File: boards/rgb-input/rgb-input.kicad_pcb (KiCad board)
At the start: 2 copper layers, 184.5 x 137 mm, 80 parts, among them J1 Conn_01x03, J10 Conn_01x03, J11 Conn_01x03, J12 Conn_01x03, J13 I2C, J14 N2K, J15 Conn_01x03, J16 Conn_01x03, J17 Conn_01x03, J18 Conn_01x03, J2 Conn_01x03, J3 Conn_01x03, J5 Conn_01x03, J6 Conn_01x03, J7 Conn_01x03, J8 Conn_01x03, J9 Conn_01x03, U1 ESP32-DEVKITC, U13 MCP1502, U2 MCP3208, U3 R-78K5.0-1.0, U4 MCP3221A0T

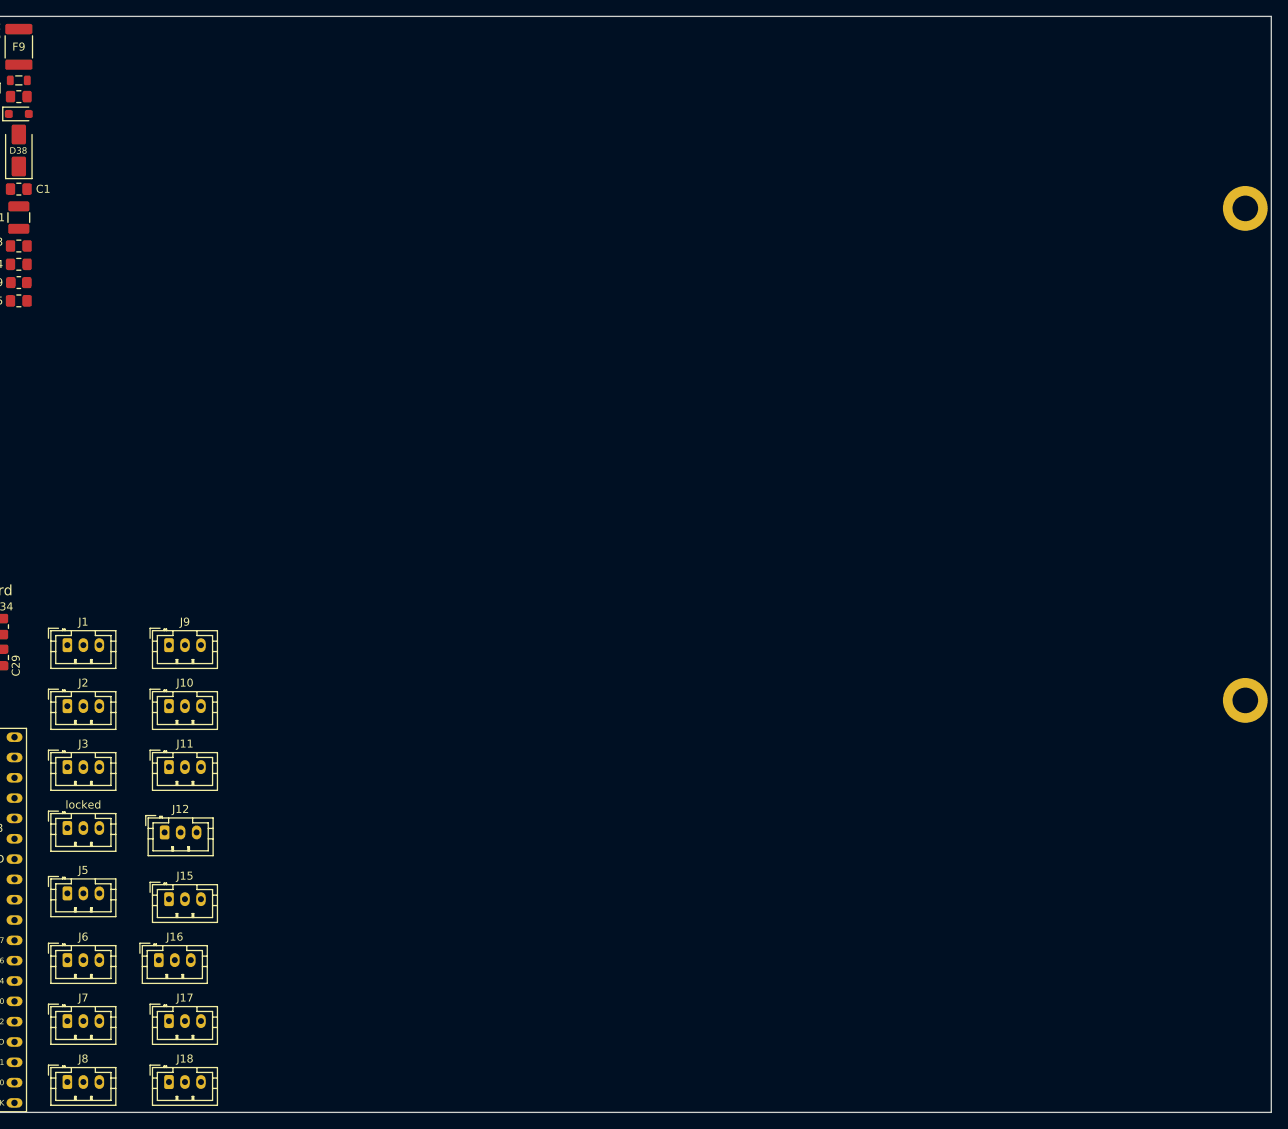
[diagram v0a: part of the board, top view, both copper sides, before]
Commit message: input board shaping up to be lit.
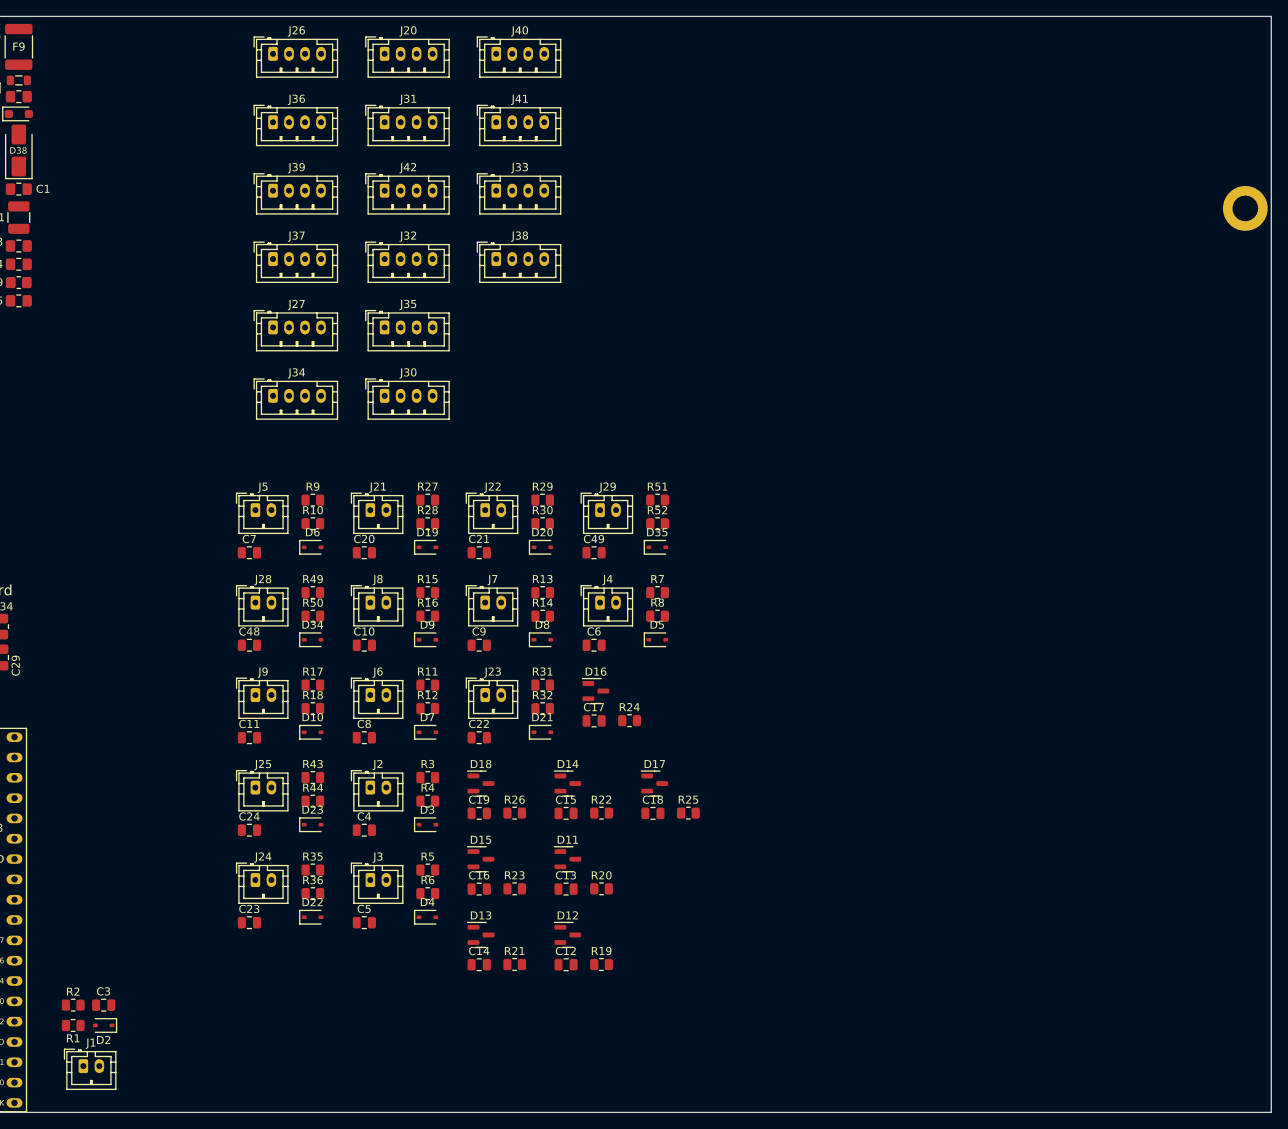
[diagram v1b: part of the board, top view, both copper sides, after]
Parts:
- removed H5: MountingHole, MountingHole:MountingHole_3.2mm_M3_DIN965_Pad
- removed J10, J11, J12, J15, J16, J17, J18, locked: Conn_01x03, Connector_JST:JST_PH_B3B-PH-K_1x03_P2.00mm_Vertical
- added C10: 0.01uf, Capacitor_SMD:C_0805_2012Metric, F.Cu at (71.1, 78.6)
- added C11: 0.01uf, Capacitor_SMD:C_0805_2012Metric, F.Cu at (56.8, 90.2)
- added C12: 0.01uf, Capacitor_SMD:C_0805_2012Metric, F.Cu at (96.3, 118.5)
- added C13: 0.01uf, Capacitor_SMD:C_0805_2012Metric, F.Cu at (96.3, 109.1)
- added C14: 0.01uf, Capacitor_SMD:C_0805_2012Metric, F.Cu at (85.5, 118.5)
- added C15: 0.01uf, Capacitor_SMD:C_0805_2012Metric, F.Cu at (96.3, 99.6)
- added C16: 0.01uf, Capacitor_SMD:C_0805_2012Metric, F.Cu at (85.5, 109.1)
- added C17: 0.01uf, Capacitor_SMD:C_0805_2012Metric, F.Cu at (99.8, 88.1)
- added C18: 0.01uf, Capacitor_SMD:C_0805_2012Metric, F.Cu at (107.2, 99.6)
- added C19: 0.01uf, Capacitor_SMD:C_0805_2012Metric, F.Cu at (85.5, 99.6)
- added C20: 0.01uf, Capacitor_SMD:C_0805_2012Metric, F.Cu at (71.1, 67.0)
- added C21: 0.01uf, Capacitor_SMD:C_0805_2012Metric, F.Cu at (85.5, 67.0)
- added C22: 0.01uf, Capacitor_SMD:C_0805_2012Metric, F.Cu at (85.5, 90.2)
- added C23: 0.01uf, Capacitor_SMD:C_0805_2012Metric, F.Cu at (56.8, 113.3)
- added C24: 0.01uf, Capacitor_SMD:C_0805_2012Metric, F.Cu at (56.8, 101.7)
- added C3: 0.01uf, Capacitor_SMD:C_0805_2012Metric, F.Cu at (38.5, 123.6)
- added C4: 0.01uf, Capacitor_SMD:C_0805_2012Metric, F.Cu at (71.1, 101.7)
- added C48: 0.01uf, Capacitor_SMD:C_0805_2012Metric, F.Cu at (56.8, 78.6)
- added C49: 0.01uf, Capacitor_SMD:C_0805_2012Metric, F.Cu at (99.8, 67.0)
- added C5: 0.01uf, Capacitor_SMD:C_0805_2012Metric, F.Cu at (71.1, 113.3)
- added C6: 0.01uf, Capacitor_SMD:C_0805_2012Metric, F.Cu at (99.8, 78.6)
- added C7: 0.01uf, Capacitor_SMD:C_0805_2012Metric, F.Cu at (56.8, 67.0)
- added C8: 0.01uf, Capacitor_SMD:C_0805_2012Metric, F.Cu at (71.1, 90.2)
- added C9: 0.01uf, Capacitor_SMD:C_0805_2012Metric, F.Cu at (85.5, 78.6)
- added D10: PESD3V3L1BA, Diode_SMD:D_SOD-323, F.Cu at (64.7, 89.5)
- added D11: BAT54S, Package_TO_SOT_SMD:SOT-23, F.Cu at (96.6, 105.4)
- added D12: BAT54S, Package_TO_SOT_SMD:SOT-23, F.Cu at (96.6, 114.8)
- added D13: BAT54S, Package_TO_SOT_SMD:SOT-23, F.Cu at (85.7, 114.8)
- added D14: BAT54S, Package_TO_SOT_SMD:SOT-23, F.Cu at (96.6, 95.9)
- added D15: BAT54S, Package_TO_SOT_SMD:SOT-23, F.Cu at (85.7, 105.4)
- added D16: BAT54S, Package_TO_SOT_SMD:SOT-23, F.Cu at (100.1, 84.3)
- added D17: BAT54S, Package_TO_SOT_SMD:SOT-23, F.Cu at (107.4, 95.9)
- added D18: BAT54S, Package_TO_SOT_SMD:SOT-23, F.Cu at (85.7, 95.9)
- added D19: PESD3V3L1BA, Diode_SMD:D_SOD-323, F.Cu at (79.0, 66.4)
- added D2: PESD3V3L1BA, Diode_SMD:D_SOD-323, F.Cu at (38.5, 126.1)
- added D20: PESD3V3L1BA, Diode_SMD:D_SOD-323, F.Cu at (93.4, 66.4)
- added D21: PESD3V3L1BA, Diode_SMD:D_SOD-323, F.Cu at (93.4, 89.5)
- added D22: PESD3V3L1BA, Diode_SMD:D_SOD-323, F.Cu at (64.7, 112.6)
- added D23: PESD3V3L1BA, Diode_SMD:D_SOD-323, F.Cu at (64.7, 101.0)
- added D3: PESD3V3L1BA, Diode_SMD:D_SOD-323, F.Cu at (79.0, 101.0)
- added D34: PESD3V3L1BA, Diode_SMD:D_SOD-323, F.Cu at (64.7, 77.9)
- added D35: PESD3V3L1BA, Diode_SMD:D_SOD-323, F.Cu at (107.7, 66.4)
- added D4: PESD3V3L1BA, Diode_SMD:D_SOD-323, F.Cu at (79.0, 112.6)
- added D5: PESD3V3L1BA, Diode_SMD:D_SOD-323, F.Cu at (107.7, 77.9)
- added D6: PESD3V3L1BA, Diode_SMD:D_SOD-323, F.Cu at (64.7, 66.4)
- added D7: PESD3V3L1BA, Diode_SMD:D_SOD-323, F.Cu at (79.0, 89.5)
- added D8: PESD3V3L1BA, Diode_SMD:D_SOD-323, F.Cu at (93.4, 77.9)
- added D9: PESD3V3L1BA, Diode_SMD:D_SOD-323, F.Cu at (79.0, 77.9)
- added J20: Conn_01x04, Connector_JST:JST_PH_B4B-PH-K_1x04_P2.00mm_Vertical, F.Cu at (73.7, 4.68)
- added J21: Conn_01x02, Connector_JST:JST_PH_B2B-PH-K_1x02_P2.00mm_Vertical, F.Cu at (71.9, 61.7)
- added J22: Conn_01x02, Connector_JST:JST_PH_B2B-PH-K_1x02_P2.00mm_Vertical, F.Cu at (86.2, 61.7)
- added J23: Conn_01x02, Connector_JST:JST_PH_B2B-PH-K_1x02_P2.00mm_Vertical, F.Cu at (86.2, 84.8)
- added J24: Conn_01x02, Connector_JST:JST_PH_B2B-PH-K_1x02_P2.00mm_Vertical, F.Cu at (57.5, 108.0)
- added J25: Conn_01x02, Connector_JST:JST_PH_B2B-PH-K_1x02_P2.00mm_Vertical, F.Cu at (57.5, 96.4)
- added J26: Conn_01x04, Connector_JST:JST_PH_B4B-PH-K_1x04_P2.00mm_Vertical, F.Cu at (59.7, 4.68)
- added J27: Conn_01x04, Connector_JST:JST_PH_B4B-PH-K_1x04_P2.00mm_Vertical, F.Cu at (59.7, 38.9)
- added J28: Conn_01x02, Connector_JST:JST_PH_B2B-PH-K_1x02_P2.00mm_Vertical, F.Cu at (57.5, 73.3)
- added J29: Conn_01x02, Connector_JST:JST_PH_B2B-PH-K_1x02_P2.00mm_Vertical, F.Cu at (100.6, 61.7)
- added J30: Conn_01x04, Connector_JST:JST_PH_B4B-PH-K_1x04_P2.00mm_Vertical, F.Cu at (73.7, 47.4)
- added J31: Conn_01x04, Connector_JST:JST_PH_B4B-PH-K_1x04_P2.00mm_Vertical, F.Cu at (73.7, 13.2)
- added J32: Conn_01x04, Connector_JST:JST_PH_B4B-PH-K_1x04_P2.00mm_Vertical, F.Cu at (73.7, 30.3)
- added J33: Conn_01x04, Connector_JST:JST_PH_B4B-PH-K_1x04_P2.00mm_Vertical, F.Cu at (87.6, 21.8)
- added J34: Conn_01x04, Connector_JST:JST_PH_B4B-PH-K_1x04_P2.00mm_Vertical, F.Cu at (59.7, 47.4)
- added J35: Conn_01x04, Connector_JST:JST_PH_B4B-PH-K_1x04_P2.00mm_Vertical, F.Cu at (73.7, 38.9)
- added J36: Conn_01x04, Connector_JST:JST_PH_B4B-PH-K_1x04_P2.00mm_Vertical, F.Cu at (59.7, 13.2)
- added J37: Conn_01x04, Connector_JST:JST_PH_B4B-PH-K_1x04_P2.00mm_Vertical, F.Cu at (59.7, 30.3)
- added J38: Conn_01x04, Connector_JST:JST_PH_B4B-PH-K_1x04_P2.00mm_Vertical, F.Cu at (87.6, 30.3)
- added J39: Conn_01x04, Connector_JST:JST_PH_B4B-PH-K_1x04_P2.00mm_Vertical, F.Cu at (59.7, 21.8)
- added J4: Conn_01x02, Connector_JST:JST_PH_B2B-PH-K_1x02_P2.00mm_Vertical, F.Cu at (100.6, 73.3)
- added J40: Conn_01x04, Connector_JST:JST_PH_B4B-PH-K_1x04_P2.00mm_Vertical, F.Cu at (87.6, 4.68)
- added J41: Conn_01x04, Connector_JST:JST_PH_B4B-PH-K_1x04_P2.00mm_Vertical, F.Cu at (87.6, 13.2)
- added J42: Conn_01x04, Connector_JST:JST_PH_B4B-PH-K_1x04_P2.00mm_Vertical, F.Cu at (73.7, 21.8)
- added R1: 1k, Resistor_SMD:R_0805_2012Metric, F.Cu at (34.7, 126.1)
- added R10: 100k, Resistor_SMD:R_0805_2012Metric, F.Cu at (64.7, 63.4)
- added R11: 1k, Resistor_SMD:R_0805_2012Metric, F.Cu at (79.1, 83.6)
- added R12: 100k, Resistor_SMD:R_0805_2012Metric, F.Cu at (79.1, 86.5)
- added R13: 1k, Resistor_SMD:R_0805_2012Metric, F.Cu at (93.4, 72.0)
- added R14: 100k, Resistor_SMD:R_0805_2012Metric, F.Cu at (93.4, 75.0)
- added R15: 1k, Resistor_SMD:R_0805_2012Metric, F.Cu at (79.1, 72.0)
- added R16: 100k, Resistor_SMD:R_0805_2012Metric, F.Cu at (79.1, 75.0)
- added R17: 1k, Resistor_SMD:R_0805_2012Metric, F.Cu at (64.7, 83.6)
- added R18: 100k, Resistor_SMD:R_0805_2012Metric, F.Cu at (64.7, 86.5)
- added R19: 1k, Resistor_SMD:R_0805_2012Metric, F.Cu at (100.8, 118.5)
- added R2: 100k, Resistor_SMD:R_0805_2012Metric, F.Cu at (34.7, 123.6)
- added R20: 1k, Resistor_SMD:R_0805_2012Metric, F.Cu at (100.8, 109.1)
- added R21: 1k, Resistor_SMD:R_0805_2012Metric, F.Cu at (89.9, 118.5)
- added R22: 1k, Resistor_SMD:R_0805_2012Metric, F.Cu at (100.8, 99.6)
- added R23: 1k, Resistor_SMD:R_0805_2012Metric, F.Cu at (89.9, 109.1)
- added R24: 1k, Resistor_SMD:R_0805_2012Metric, F.Cu at (104.3, 88.0)
- added R25: 1k, Resistor_SMD:R_0805_2012Metric, F.Cu at (111.6, 99.6)
- added R26: 1k, Resistor_SMD:R_0805_2012Metric, F.Cu at (89.9, 99.6)
- added R27: 1k, Resistor_SMD:R_0805_2012Metric, F.Cu at (79.1, 60.5)
- added R28: 100k, Resistor_SMD:R_0805_2012Metric, F.Cu at (79.1, 63.4)
- added R29: 1k, Resistor_SMD:R_0805_2012Metric, F.Cu at (93.4, 60.5)
- added R3: 1k, Resistor_SMD:R_0805_2012Metric, F.Cu at (79.1, 95.1)
- added R30: 100k, Resistor_SMD:R_0805_2012Metric, F.Cu at (93.4, 63.4)
- added R31: 1k, Resistor_SMD:R_0805_2012Metric, F.Cu at (93.4, 83.6)
- added R32: 100k, Resistor_SMD:R_0805_2012Metric, F.Cu at (93.4, 86.5)
- added R35: 1k, Resistor_SMD:R_0805_2012Metric, F.Cu at (64.7, 106.7)
- added R36: 100k, Resistor_SMD:R_0805_2012Metric, F.Cu at (64.7, 109.7)
- added R4: 100k, Resistor_SMD:R_0805_2012Metric, F.Cu at (79.1, 98.1)
- added R43: 1k, Resistor_SMD:R_0805_2012Metric, F.Cu at (64.7, 95.1)
- added R44: 100k, Resistor_SMD:R_0805_2012Metric, F.Cu at (64.7, 98.1)
- added R49: 1k, Resistor_SMD:R_0805_2012Metric, F.Cu at (64.7, 72.0)
- added R5: 1k, Resistor_SMD:R_0805_2012Metric, F.Cu at (79.1, 106.7)
- added R50: 100k, Resistor_SMD:R_0805_2012Metric, F.Cu at (64.7, 75.0)
- added R51: 1k, Resistor_SMD:R_0805_2012Metric, F.Cu at (107.8, 60.5)
- added R52: 100k, Resistor_SMD:R_0805_2012Metric, F.Cu at (107.8, 63.4)
- added R6: 100k, Resistor_SMD:R_0805_2012Metric, F.Cu at (79.1, 109.7)
- added R7: 1k, Resistor_SMD:R_0805_2012Metric, F.Cu at (107.8, 72.0)
- added R8: 100k, Resistor_SMD:R_0805_2012Metric, F.Cu at (107.8, 75.0)
- added R9: 1k, Resistor_SMD:R_0805_2012Metric, F.Cu at (64.7, 60.5)
- J1, J2, J3, J5, J6, J7, J8, J9: value Conn_01x03 -> Conn_01x02; footprint Connector_JST:JST_PH_B3B-PH-K_1x03_P2.00mm_Vertical -> Connector_JST:JST_PH_B2B-PH-K_1x02_P2.00mm_Vertical
- moved J7 73.9 mm to (86.2, 73.3)
- moved J8 70.9 mm to (71.9, 73.3)
- moved J5 53.4 mm to (57.5, 61.7)
- moved J1 52.7 mm to (36.0, 131.2)
- moved J6 50.3 mm to (71.9, 84.8)
- moved J3 40.4 mm to (71.9, 108.0)
- moved J2 39.2 mm to (71.9, 96.4)
- moved J9 12.5 mm to (57.5, 84.8)
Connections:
- J1 pad 1: unconnected-(J1-Pin_1-Pad1) -> Net-(D2-A2)
- J1 pad 2: unconnected-(J1-Pin_2-Pad2) -> GNDD
- J2 pad 1: unconnected-(J2-Pin_1-Pad1) -> Net-(D3-A2)
- J2 pad 2: unconnected-(J2-Pin_2-Pad2) -> GNDD
- J3 pad 1: unconnected-(J3-Pin_1-Pad1) -> Net-(D4-A2)
- J3 pad 2: unconnected-(J3-Pin_2-Pad2) -> GNDD
- J5 pad 1: unconnected-(J5-Pin_1-Pad1) -> Net-(D6-A2)
- J5 pad 2: unconnected-(J5-Pin_2-Pad2) -> GNDD
- J6 pad 1: unconnected-(J6-Pin_1-Pad1) -> Net-(D7-A2)
- J6 pad 2: unconnected-(J6-Pin_2-Pad2) -> GNDD
- J7 pad 1: unconnected-(J7-Pin_1-Pad1) -> Net-(D8-A2)
- J7 pad 2: unconnected-(J7-Pin_2-Pad2) -> GNDD
- J8 pad 1: unconnected-(J8-Pin_1-Pad1) -> Net-(D9-A2)
- J8 pad 2: unconnected-(J8-Pin_2-Pad2) -> GNDD
- J9 pad 1: unconnected-(J9-Pin_1-Pad1) -> Net-(D10-A2)
- J9 pad 2: unconnected-(J9-Pin_2-Pad2) -> GNDD
- U1 pad 10: unconnected-(U1-GPIO26-Pad10) -> /Input Switch7/INPUT
- U1 pad 11: unconnected-(U1-GPIO27-Pad11) -> /Input Switch8/INPUT
- U1 pad 12: unconnected-(U1-GPIO14-Pad12) -> /Input Switch9/INPUT
- U1 pad 13: unconnected-(U1-GPIO12-Pad13) -> /Input Switch10/INPUT
- U1 pad 15: unconnected-(U1-GPIO13-Pad15) -> /Input Switch11/INPUT
- U1 pad 24: unconnected-(U1-GPIO2-Pad24) -> /Input Switch12/INPUT
- U1 pad 26: CAN_RX -> /Input Switch13/INPUT
- U1 pad 27: unconnected-(U1-GPIO16-Pad27) -> /Input Switch14/INPUT
- U1 pad 29: CAN_TX -> /Input Switch15/INPUT
- U1 pad 3: unconnected-(U1-GPIO36-Pad3) -> /Input Switch0/INPUT
- U1 pad 4: unconnected-(U1-GPIO39-Pad4) -> /Input Switch1/INPUT
- U1 pad 5: unconnected-(U1-GPIO34-Pad5) -> /Input Switch2/INPUT
- U1 pad 6: unconnected-(U1-GPIO35-Pad6) -> /Input Switch3/INPUT
- U1 pad 7: unconnected-(U1-GPIO32-Pad7) -> /Input Switch4/INPUT
- U1 pad 8: unconnected-(U1-GPIO33-Pad8) -> /Input Switch5/INPUT
- U1 pad 9: unconnected-(U1-GPIO25-Pad9) -> /Input Switch6/INPUT
- U2 pad 1: /ADC/A0 -> /ADC Input/INPUT
- U2 pad 2: /ADC/A1 -> /ADC Input1/INPUT
- U2 pad 3: /ADC/A2 -> /ADC Input2/INPUT
- U2 pad 4: /ADC/A3 -> /ADC Input3/INPUT
- U2 pad 5: /ADC/A4 -> /ADC Input4/INPUT
- U2 pad 6: /ADC/A5 -> /ADC Input5/INPUT
- U2 pad 7: /ADC/A6 -> /ADC Input6/INPUT
- U2 pad 8: /ADC/A7 -> /ADC Input7/INPUT

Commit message: some adc changes and then rerouting
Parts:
- removed C38, C40, C41: 33pF, Capacitor_SMD:C_0805_2012Metric_Pad1.18x1.45mm_HandSolder
- removed C39, C42: 10uF, Capacitor_SMD:C_0805_2012Metric_Pad1.18x1.45mm_HandSolder
- removed D29, D30, D31: PESD5V0L1BA, Diode_SMD:D_SOD-323_HandSoldering
- removed FB4, FB5, FB6: GZ2012D601TF, Inductor_SMD:L_0805_2012Metric
- removed J42: Conn_01x04, Connector_JST:JST_PH_B4B-PH-K_1x04_P2.00mm_Vertical
- removed U4: MCP3221A0T, Package_TO_SOT_SMD:SOT-23-5
- added C25: 10uF, Capacitor_SMD:C_0805_2012Metric, F.Cu at (-22.4, 36.6)
- added C26: 10uF, Capacitor_SMD:C_0805_2012Metric, F.Cu at (-22.4, 51.2)
- added D39: BAT54S, Package_TO_SOT_SMD:SOT-23, F.Cu at (-15.7, 50.5)
- added JP1: SolderJumper_2_Open, Jumper:SolderJumper-2_P1.3mm_Open_RoundedPad1.0x1.5mm, F.Cu at (-11.1, 50.0)
- added R45: 10k, Resistor_SMD:R_0805_2012Metric, F.Cu at (-22.4, 30.6)
- added R46: 3.3k, Resistor_SMD:R_0805_2012Metric, F.Cu at (-22.4, 33.6)
- added R47: 10k, Resistor_SMD:R_0805_2012Metric, F.Cu at (-22.4, 45.3)
- added R48: 3.3k, Resistor_SMD:R_0805_2012Metric, F.Cu at (-22.4, 48.2)
- added U15: MCP3425A0T-ECH, Package_TO_SOT_SMD:SOT-23-6, F.Cu at (-15.6, 46.0)
- added U5: TLC5947DAP, Package_SO:HTSSOP-32-1EP_6.1x11mm_P0.65mm_EP5.2x11mm_Mask4.11x4.36mm_ThermalVias, F.Cu at (-29.7, 35.5)
- added U6: TLC5947DAP, Package_SO:HTSSOP-32-1EP_6.1x11mm_P0.65mm_EP5.2x11mm_Mask4.11x4.36mm_ThermalVias, F.Cu at (-29.7, 50.1)
- C37: value 33pF -> 10uF
- D1, D27, D28: value PESD5V0L1BA -> PESD3V3L1BA
- J14: value N2K -> Conn_01x04; footprint Connector_PinHeader_2.54mm:PinHeader_1x04_P2.54mm_Vertical -> Connector_JST:JST_PH_B4B-PH-K_1x04_P2.00mm_Vertical
- R33: value 130K 0.1% -> 300K 0.1%
- R34: value 15K 0.1% -> 22K 0.1%
- moved J14 71.7 mm to (73.6, 21.4), turned to 0 degrees
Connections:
- C29 pad 1: +3.3V -> ESP32_5V
- C37 pad 1: Net-(D29-A2) -> REF_3V3
- C37 pad 2: GNDD -> GNDA
- J14 pad 1: Net-(D29-A2) -> +5V
- J14 pad 2: Net-(D30-A2) -> /LEDS/LED Driver1/OUT6
- J14 pad 3: GNDD -> /LEDS/LED Driver1/OUT7
- J14 pad 4: Net-(D31-A2) -> /LEDS/LED Driver1/OUT8
- J20 pad 2: /RGB Output0/RED -> /LEDS/LED Driver1/OUT15
- J20 pad 3: /RGB Output0/GREEN -> /LEDS/LED Driver1/OUT16
- J20 pad 4: /RGB Output0/BLUE -> /LEDS/LED Driver1/OUT17
- J26 pad 2: /RGB Output1/RED -> /LEDS/LED Driver1/OUT3
- J26 pad 3: /RGB Output1/GREEN -> /LEDS/LED Driver1/OUT4
- J26 pad 4: /RGB Output1/BLUE -> /LEDS/LED Driver1/OUT5
- J27 pad 2: /RGB Output2/RED -> /LEDS/LED Driver/OUT6
- J27 pad 3: /RGB Output2/GREEN -> /LEDS/LED Driver/OUT7
- J27 pad 4: /RGB Output2/BLUE -> /LEDS/LED Driver/OUT8
- J30 pad 2: /RGB Output3/RED -> /LEDS/LED Driver1/OUT18
- J30 pad 3: /RGB Output3/GREEN -> /LEDS/LED Driver1/OUT19
- J30 pad 4: /RGB Output3/BLUE -> /LEDS/LED Driver1/OUT20
- J31 pad 2: /RGB Output5/RED -> /LEDS/LED Driver/OUT15
- J31 pad 3: /RGB Output5/GREEN -> /LEDS/LED Driver/OUT16
- J31 pad 4: /RGB Output5/BLUE -> /LEDS/LED Driver/OUT17
- J32 pad 2: /RGB Output4/RED -> /LEDS/LED Driver1/OUT12
- J32 pad 3: /RGB Output4/GREEN -> /LEDS/LED Driver1/OUT13
- J32 pad 4: /RGB Output4/BLUE -> /LEDS/LED Driver1/OUT14
- J33 pad 2: /RGB Output7/RED -> /LEDS/LED Driver/OUT3
- J33 pad 3: /RGB Output7/GREEN -> /LEDS/LED Driver/OUT4
- J33 pad 4: /RGB Output7/BLUE -> /LEDS/LED Driver/OUT5
- J34 pad 2: /RGB Output6/RED -> /LEDS/LED Driver/OUT18
- J34 pad 3: /RGB Output6/GREEN -> /LEDS/LED Driver/OUT19
- J34 pad 4: /RGB Output6/BLUE -> /LEDS/LED Driver/OUT20
- J35 pad 2: /RGB Output9/RED -> /LEDS/LED Driver/OUT12
- J35 pad 3: /RGB Output9/GREEN -> /LEDS/LED Driver/OUT13
- J35 pad 4: /RGB Output9/BLUE -> /LEDS/LED Driver/OUT14
- J36 pad 2: /RGB Output8/RED -> /LEDS/LED Driver/OUT9
- J36 pad 3: /RGB Output8/GREEN -> /LEDS/LED Driver/OUT10
- J36 pad 4: /RGB Output8/BLUE -> /LEDS/LED Driver/OUT11
- J37 pad 2: /RGB Output11/RED -> /LEDS/LED Driver1/OUT9
- J37 pad 3: /RGB Output11/GREEN -> /LEDS/LED Driver1/OUT10
- J37 pad 4: /RGB Output11/BLUE -> /LEDS/LED Driver1/OUT11
- J38 pad 2: /RGB Output10/RED -> /LEDS/LED Driver/OUT21
- J38 pad 3: /RGB Output10/GREEN -> /LEDS/LED Driver/OUT22
- J38 pad 4: /RGB Output10/BLUE -> /LEDS/LED Driver/OUT23
- J39 pad 2: /RGB Output13/RED -> /LEDS/LED Driver1/OUT21
- J39 pad 3: /RGB Output13/GREEN -> /LEDS/LED Driver1/OUT22
- J39 pad 4: /RGB Output13/BLUE -> /LEDS/LED Driver1/OUT23
- J40 pad 2: /RGB Output12/RED -> /LEDS/LED Driver1/OUT0
- J40 pad 3: /RGB Output12/GREEN -> /LEDS/LED Driver1/OUT1
- J40 pad 4: /RGB Output12/BLUE -> /LEDS/LED Driver1/OUT2
- J41 pad 2: /RGB Output15/RED -> /LEDS/LED Driver/OUT0
- J41 pad 3: /RGB Output15/GREEN -> /LEDS/LED Driver/OUT1
- J41 pad 4: /RGB Output15/BLUE -> /LEDS/LED Driver/OUT2
- U1 pad 19: unconnected-(U1-5V0-Pad19) -> ESP32_VIN
- U13 pad 4: +3.3V -> ESP32_5V
- U13 pad 6: +3.3V -> ESP32_5V
